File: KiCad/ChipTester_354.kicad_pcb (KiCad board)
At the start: 2 copper layers, 11 parts, among them U3 MCP6002-xP

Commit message: added footprints to schematic
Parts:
- removed U3: MCP6002-xP, Package_SO:SOIC-8_3.9x4.9mm_P1.27mm
- added C1: 0.33 µF, Capacitor_SMD:C_0201_0603Metric, F.Cu at (23.2, 61.0)
- added C2: 0.1 µF, Capacitor_SMD:C_0201_0603Metric, F.Cu at (23.2, 66.0)
- added D3: BLU, Diode_SMD:D_0201_0603Metric, F.Cu at (40.3, 66.0)
- added D4: WHT, Diode_SMD:D_0201_0603Metric, F.Cu at (39.6, 71.1)
- added D5: BLU, Diode_SMD:D_0201_0603Metric, F.Cu at (39.6, 76.2)
- added D6: WHT, Diode_SMD:D_0201_0603Metric, F.Cu at (39.6, 81.3)
- added R1: 510, Resistor_SMD:R_0201_0603Metric, F.Cu at (23.2, 81.3)
- added R2: 510, Resistor_SMD:R_0201_0603Metric, F.Cu at (23.2, 86.4)
- added U1: L7805, Package_TO_SOT_THT:TO-218-3_Vertical, F.Cu at (35.2, 59.1)
- added U2: AD623/INA126, Package_DIP:DIP-8_W7.62mm_Socket, F.Cu at (116.1, 39.2)
- added U6: TLE2426xP, Package_DIP:DIP-8_W7.62mm, F.Cu at (115.6, 25.4)
- added U7: TLE2426xP, Package_DIP:DIP-8_W7.62mm, F.Cu at (126.4, 25.4)
- added U8: TLE2426xP, Package_DIP:DIP-8_W7.62mm, F.Cu at (137.2, 25.4)
- R7: value 10k -> 20k
- R9: value 10k -> 7.5k
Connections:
- net /Wave Generator/WAVE renamed /WAVE

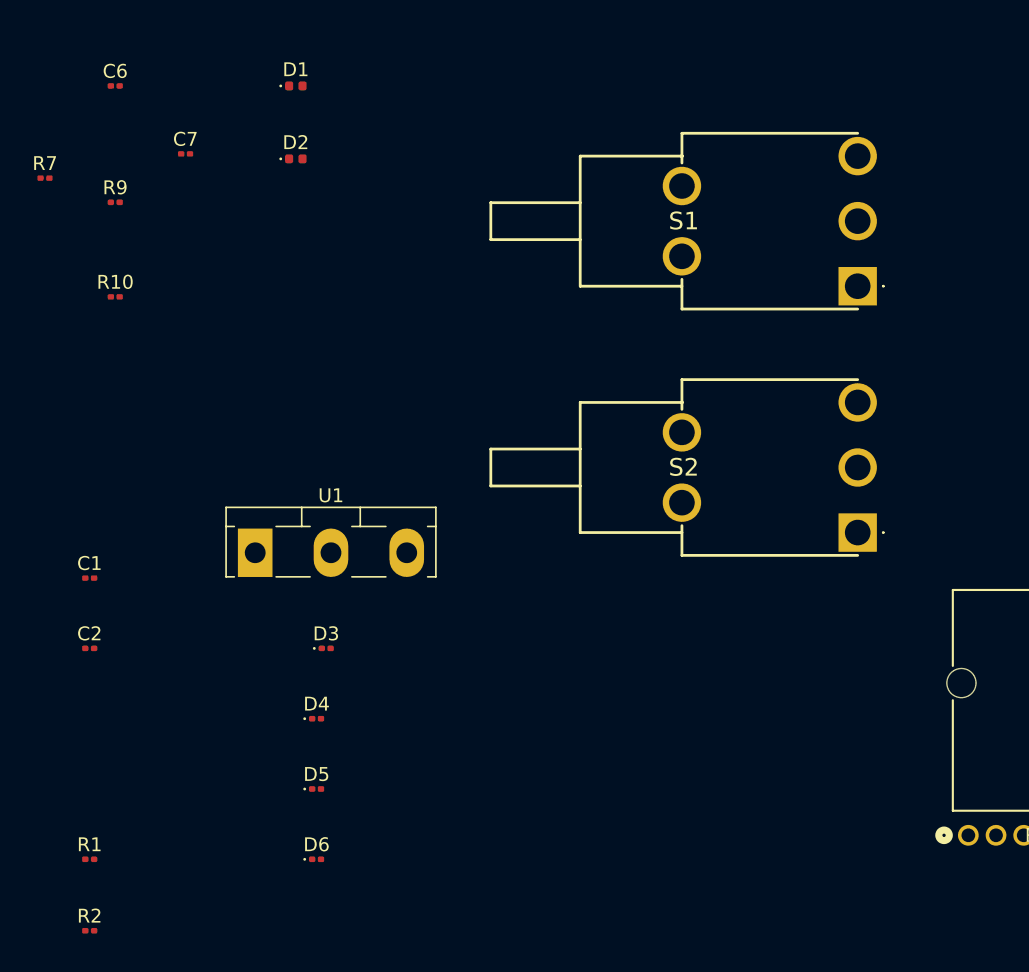
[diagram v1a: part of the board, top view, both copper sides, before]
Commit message: updated footprint to be all THT, battery holder still not there
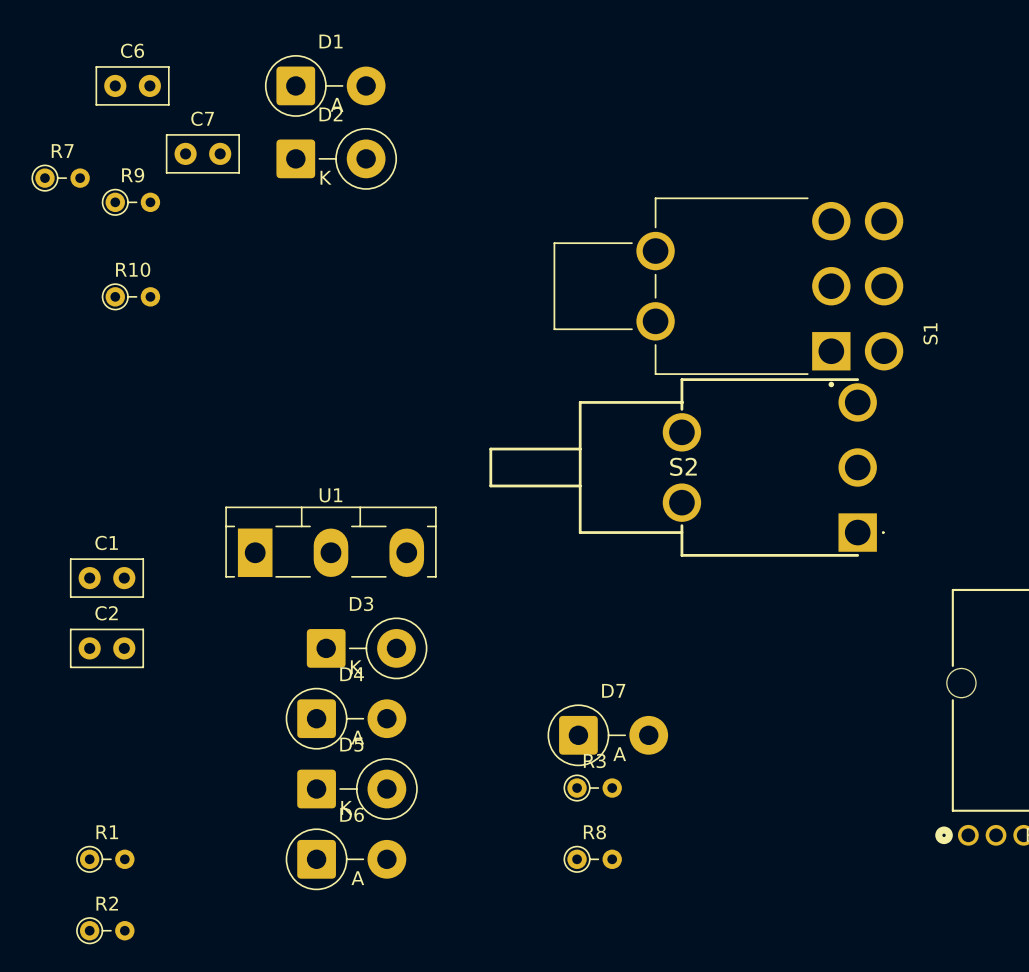
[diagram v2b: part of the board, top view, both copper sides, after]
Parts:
- added D7: GRN, Diode_THT:D_5W_P5.08mm_Vertical_AnodeUp, F.Cu at (58.5, 72.3)
- added R3: 1k, Resistor_THT:R_Axial_DIN0204_L3.6mm_D1.6mm_P2.54mm_Vertical, F.Cu at (58.4, 76.1)
- added R8: 20k, Resistor_THT:R_Axial_DIN0204_L3.6mm_D1.6mm_P2.54mm_Vertical, F.Cu at (58.4, 81.3)
- C1, C2, C6, C7: footprint Capacitor_SMD:C_0201_0603Metric -> Capacitor_THT:C_Disc_D5.0mm_W2.5mm_P2.50mm
- D1: footprint Diode_SMD:D_0402_1005Metric -> Diode_THT:D_5W_P5.08mm_Vertical_AnodeUp
- D2: footprint Diode_SMD:D_0402_1005Metric -> Diode_THT:D_5W_P5.08mm_Vertical_KathodeUp
- D3, D5: footprint Diode_SMD:D_0201_0603Metric -> Diode_THT:D_5W_P5.08mm_Vertical_KathodeUp
- D4, D6: footprint Diode_SMD:D_0201_0603Metric -> Diode_THT:D_5W_P5.08mm_Vertical_AnodeUp
- R1, R10, R2, R7, R9: footprint Resistor_SMD:R_0201_0603Metric -> Resistor_THT:R_Axial_DIN0204_L3.6mm_D1.6mm_P2.54mm_Vertical
- S1: value 100SP3T2B4M6RE -> 100DP1T2B4M6QE; footprint 100SP3T2B4M6RE:100SP3T2B4M6RE -> 100DP1T2B4M6QE:SW_100DP1T2B4M6QE
- turned S1 to 90 degrees
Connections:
- D4 pad 1: Net-(D3-A) -> /CHIP_GND
- D4 pad 2: /CHIP_GND -> Net-(D3-A)
- D6 pad 1: Net-(D5-A) -> /CHIP_GND
- D6 pad 2: /CHIP_GND -> Net-(D5-A)
- S1 pad 1: unconnected-(S1-N1-Pad1) -> +9V
- S1 pad 3: +9V -> unconnected-(S1-Pad3)

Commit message: Some TP -> Headers, added footprints, fixed battery footprint, started layout of board.
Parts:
- removed U6, U7, U8: TLE2426xP, Package_DIP:DIP-8_W7.62mm
- added BT_H1: BH9VPC, BH9VPC:BAT_BH9VPC, B.Cu at (240.5, 55.0)
- added C3: 0.1 µF, Capacitor_THT:C_Disc_D5.0mm_W2.5mm_P2.50mm, F.Cu at (-142.4, 102.9)
- added C4: 1 µF, Capacitor_THT:CP_Radial_D5.0mm_P2.00mm, F.Cu at (-3.41, -54.3)
- added C5: 1 µF, Capacitor_THT:CP_Radial_D5.0mm_P2.00mm, F.Cu at (-3.41, -47.7)
- added D10: BLU, Diode_THT:D_5W_P5.08mm_Vertical_KathodeUp, F.Cu at (-127.7, 5.95)
- added D11: WHT, Diode_THT:D_5W_P5.08mm_Vertical_AnodeUp, F.Cu at (-127.1, 11.4)
- added D12: BLU, Diode_THT:D_5W_P5.08mm_Vertical_KathodeUp, F.Cu at (-127.7, 16.9)
- added D13: WHT, Diode_THT:D_5W_P5.08mm_Vertical_AnodeUp, F.Cu at (-127.1, 22.4)
- added D8: BLU, Diode_THT:D_5W_P5.08mm_Vertical_KathodeUp, F.Cu at (-127.7, -4.99)
- added D9: WHT, Diode_THT:D_5W_P5.08mm_Vertical_AnodeUp, F.Cu at (-127.1, 0.48)
- added H1: MountingHole, MountingHole:MountingHole_3.2mm_M3, F.Cu at (-9.90, -35.4)
- added R11: 510, Resistor_THT:R_Axial_DIN0204_L3.6mm_D1.6mm_P2.54mm_Vertical, F.Cu at (-118.3, 12.0)
- added R4: 20k, Resistor_THT:R_Axial_DIN0204_L3.6mm_D1.6mm_P2.54mm_Vertical, F.Cu at (-104.0, 90.7)
- added R5: 50k, PRS12R_4025K_103B1:PRS12R-4_BRN, F.Cu at (202.7, -27.9)
- added TP1: VBATT-, TestPoint:TestPoint_Pad_D2.0mm, F.Cu at (-11.8, -55.5)
- added TP10: MCP_Out, Connector_PinSocket_2.54mm:PinSocket_1x03_P2.54mm_Vertical, F.Cu at (5.18, -55.2)
- added TP2: VBATT+, TestPoint:TestPoint_Pad_D2.0mm, F.Cu at (-11.8, -51.5)
- added TP3: 4.5V, TestPoint:TestPoint_Pad_D2.0mm, F.Cu at (-11.8, -47.4)
- added TP4: 5V+, TestPoint:TestPoint_Pad_D2.0mm, F.Cu at (-11.8, -43.4)
- added TP5: 0V (5V), TestPoint:TestPoint_Pad_D2.0mm, F.Cu at (-7.80, -55.5)
- added TP6: 4.5/2.25V VGND, TestPoint:TestPoint_Pad_D2.0mm, F.Cu at (-7.80, -51.5)
- added TP7: 2.5V VGND, TestPoint:TestPoint_Pad_D2.0mm, F.Cu at (-7.80, -47.4)
- added TP8: AD_Out, Connector_PinSocket_2.54mm:PinSocket_1x02_P2.54mm_Vertical, F.Cu at (-1.60, -37.0)
- added TP9: Wave, Connector_PinSocket_2.54mm:PinSocket_1x02_P2.54mm_Vertical, F.Cu at (5.00, -37.0)
- added U3: TLE2426xP, Package_DIP:DIP-8_W7.62mm, F.Cu at (-142.8, 91.2)
- added U4: TLE2426xP, Package_DIP:DIP-8_W7.62mm, F.Cu at (-132.0, 91.2)
- added U5: MCP6002-xP, Package_DIP:DIP-8_W7.62mm, F.Cu at (-95.9, 91.2)
- added U_T1: AD623/INA126, Package_DIP:DIP-8_W7.62mm_Socket, F.Cu at (165.7, 48.7)
- added U_T2: MCP6002-xP, Package_DIP:DIP-8_W7.62mm_Socket, F.Cu at (112.4, 60.2)
- C1: value 0.33 µF -> 1 µF; footprint Capacitor_THT:C_Disc_D5.0mm_W2.5mm_P2.50mm -> Capacitor_THT:CP_Radial_D5.0mm_P2.00mm
- C2: value 0.1 µF -> 0.33 µF
- D1: value 2.5V -> GRN
- D2: value 2.5V -> BLU
- D3, D5: value BLU -> WHT; footprint Diode_THT:D_5W_P5.08mm_Vertical_KathodeUp -> Diode_THT:D_5W_P5.08mm_Vertical_AnodeUp
- D4: value WHT -> BLU; footprint Diode_THT:D_5W_P5.08mm_Vertical_AnodeUp -> Diode_THT:D_5W_P5.08mm_Vertical_KathodeUp
- D6: value WHT -> 2.5V; footprint Diode_THT:D_5W_P5.08mm_Vertical_AnodeUp -> Diode_THT:D_5W_P5.08mm_Vertical_KathodeUp
- D7: value GRN -> 2.5V
- R1: value 510 -> 1k
- R10: value 3.3k -> 510
- R3: value 1k -> 510
- R6: value 50k -> 20k; footprint PRS12R_4025K_103B1:PRS12R-4_BRN -> Resistor_THT:R_Axial_DIN0204_L3.6mm_D1.6mm_P2.54mm_Vertical
- R7: value 20k -> 7.5k
- R8: value 20k -> 3.3k
- R9: value 7.5k -> 510
- U1: value L7805 -> TLE2426xP; footprint Package_TO_SOT_THT:TO-218-3_Vertical -> Package_DIP:DIP-8_W7.62mm
- U2: value AD623/INA126 -> L7805; footprint Package_DIP:DIP-8_W7.62mm_Socket -> Package_TO_SOT_THT:TO-218-3_Vertical
- moved D1 181.1 mm to (219.2, 26.0)
- moved U1 171.8 mm to (204.3, 29.2), turned to -90 degrees
- moved S1 160.6 mm to (239.1, 31.2), turned to -90 degrees
- moved S2 151.8 mm to (172.7, -61.5), turned to 90 degrees
- moved R10 146.8 mm to (-118.3, 8.83)
- moved R9 146.1 mm to (-118.3, 5.68)
- moved U2 79.3 mm to (119.5, -40.0), turned to 90 degrees
- moved D2 35.8 mm to (38.1, 66.5)
- moved D6 10.9 mm to (34.7, 91.0)
- moved D3 7.74 mm to (38.2, 73.5)
- moved D4 7.74 mm to (37.5, 78.6)
- moved D5 7.74 mm to (37.5, 83.7)
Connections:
- C1 pad 1: +9V -> GND
- C1 pad 2: GND -> Net-(U1-NOISE_REDUCTION)
- C2 pad 1: +5V -> +9V
- C7 pad 1: Net-(U4A-+) -> Net-(U5A-+)
- C7 pad 2: /PWR Supply/2.5V VGND -> /2.5 VGND
- D1 pad 1: Net-(D1-K) -> GND
- D2 pad 1: /WAVE -> /CHIP_GND
- D2 pad 2: Net-(D1-A) -> Net-(D2-A)
- D3 pad 2: Net-(D3-A) -> Net-(D2-A)
- D4 pad 2: Net-(D3-A) -> Net-(D4-A)
- D5 pad 2: Net-(D5-A) -> Net-(D4-A)
- D6 pad 1: /CHIP_GND -> /WAVE
- D6 pad 2: Net-(D5-A) -> Net-(D6-A)
- D7 pad 1: GND -> Net-(D7-K)
- D7 pad 2: Net-(D7-A) -> Net-(D6-A)
- R1 pad 1: /WAVE -> +9V
- R1 pad 2: Net-(D3-A) -> Net-(D1-A)
- R10 pad 1: Net-(D1-K) -> Net-(D10-A)
- R10 pad 2: /PWR Supply/2.5V VGND -> /MCP6002 and IF353/MCPA_O
- R2 pad 1: Net-(D5-A) -> /WAVE
- R2 pad 2: Net-(R2-Pad2) -> Net-(D2-A)
- R3 pad 1: +9V -> Net-(D4-A)
- R3 pad 2: Net-(D7-A) -> /AD623 and INA126/AD_O
- R6 pad 1: Net-(R6-Pad1) -> Net-(R5-Pad5)
- R6 pad 2: Net-(U4A-+) -> /2.5 VGND
- R7 pad 1: Net-(C6-Pad2) -> /WAVE
- R7 pad 2: Net-(R6-Pad1) -> Net-(D7-K)
- R8 pad 1: Net-(R6-Pad5) -> Net-(D7-K)
- R8 pad 2: /PWR Supply/2.5V VGND -> /2.5 VGND
- R9 pad 1: /WAVE -> Net-(D8-A)
- R9 pad 2: Net-(D1-K) -> /WAVE
- S1 pad 1: +9V -> unconnected-(S1-Pad1)
- S1 pad 3: unconnected-(S1-Pad3) -> +9V
- S1 pad 4: GND -> unconnected-(S1-Pad4)
- S1 pad 6: unconnected-(S1-Pad6) -> GND
- S1 pad S1: (no net) -> unconnected-(S1-PadS1)
- S1 pad S2: (no net) -> unconnected-(S1-PadS2)
- U1 pad 1: +9V -> /PWR Supply/VDIV
- U1 pad 3: +5V -> +9V
- U2 pad 1: unconnected-(U2-Rg-Pad1) -> +9V
- U2 pad 2: unconnected-(U2---Pad2) -> GND
- U2 pad 3: /WAVE -> +5V

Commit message: Made the board :D
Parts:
- added H2: MountingHole, MountingHole:MountingHole_3.2mm_M3, F.Cu at (68.9, 111.5)
- added H3: MountingHole, MountingHole:MountingHole_3.2mm_M3, F.Cu at (68.9, 57.0)
- added H4: MountingHole, MountingHole:MountingHole_3.2mm_M3, F.Cu at (233.9, 111.5)
- D1, D11, D13, D3, D5, D9: footprint Diode_THT:D_5W_P5.08mm_Vertical_AnodeUp -> LED_THT:LED_D5.0mm
- D10, D12, D2, D4, D8: footprint Diode_THT:D_5W_P5.08mm_Vertical_KathodeUp -> LED_THT:LED_D5.0mm
- D6: footprint Diode_THT:D_5W_P5.08mm_Vertical_KathodeUp -> Diode_THT:D_DO-35_SOD27_P7.62mm_Horizontal
- D7: footprint Diode_THT:D_5W_P5.08mm_Vertical_AnodeUp -> Diode_THT:D_DO-35_SOD27_P7.62mm_Horizontal
- R1, R10, R11, R2, R3, R4, R6, R7, R8, R9: footprint Resistor_THT:R_Axial_DIN0204_L3.6mm_D1.6mm_P2.54mm_Vertical -> Resistor_THT:R_Axial_DIN0207_L6.3mm_D2.5mm_P7.62mm_Horizontal
- TP1: moved to B.Cu
- U2: footprint Package_TO_SOT_THT:TO-218-3_Vertical -> Package_TO_SOT_THT:TO-218-3_Horizontal_TabDown
- moved C3 355.0 mm to (209.9, 58.2), turned to -90 degrees
- moved U4 296.7 mm to (163.7, 66.3), turned to 180 degrees
- moved R4 272.0 mm to (167.9, 85.5), turned to 180 degrees
- moved U5 267.4 mm to (171.2, 79.6)
- moved U3 260.9 mm to (117.4, 71.8), turned to 180 degrees
- moved H1 260.7 mm to (233.9, 57.0)
- moved TP1 248.2 mm to (200.4, 73.2)
- moved D9 240.1 mm to (87.8, 107.5)
- moved D13 240.1 mm to (97.3, 107.5)
- moved D12 240.0 mm to (97.3, 100.5)
- moved R11 240.0 mm to (103.4, 104.0), turned to 90 degrees
- moved D8 239.9 mm to (87.8, 100.5)
- moved R9 233.8 mm to (93.9, 104.0), turned to 90 degrees
- moved D11 226.8 mm to (78.3, 107.5)
- moved D10 226.7 mm to (78.3, 100.5)
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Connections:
- TP10 pad 1: /BATT- -> GND
- U_T2 pad 4: /BATT- -> GND
- U_T2 pad 8: /BATT+ -> +9V
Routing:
- net +9V: track 0.00 -> 159.6 mm
- net /2.5 VGND: track 0.00 -> 131.3 mm
- net /WAVE: track 0.00 -> 115.9 mm
- net +5V: track 0.00 -> 76.0 mm
- net /CHIP_GND: track 0.00 -> 59.5 mm
- net /PWR Supply/VDIV: track 0.00 -> 47.9 mm
- net Net-(D7-K): track 0.00 -> 39.8 mm
- net /BATT-: track 0.00 -> 38.9 mm
- net Net-(U5A-+): track 0.00 -> 31.0 mm
- net /MCP6002 and IF353/MCPA_O: track 0.00 -> 29.8 mm
- net /MCP6002 and IF353/MCPB_O: track 0.00 -> 29.6 mm
- net /CHIP+: track 0.00 -> 26.5 mm
- net Net-(D2-A): track 0.00 -> 24.3 mm
- net /BATT+: track 0.00 -> 22.1 mm
- net /AD623 and INA126/AD_O: track 0.00 -> 21.3 mm
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- added copper zone on B.Cu, net GND
- added copper zone on F.Cu, net GND
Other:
- board outline added: 172 x 61.5 mm
- board text added: "AD623 INA126"
- board text added: "MCP6002 & LF353"

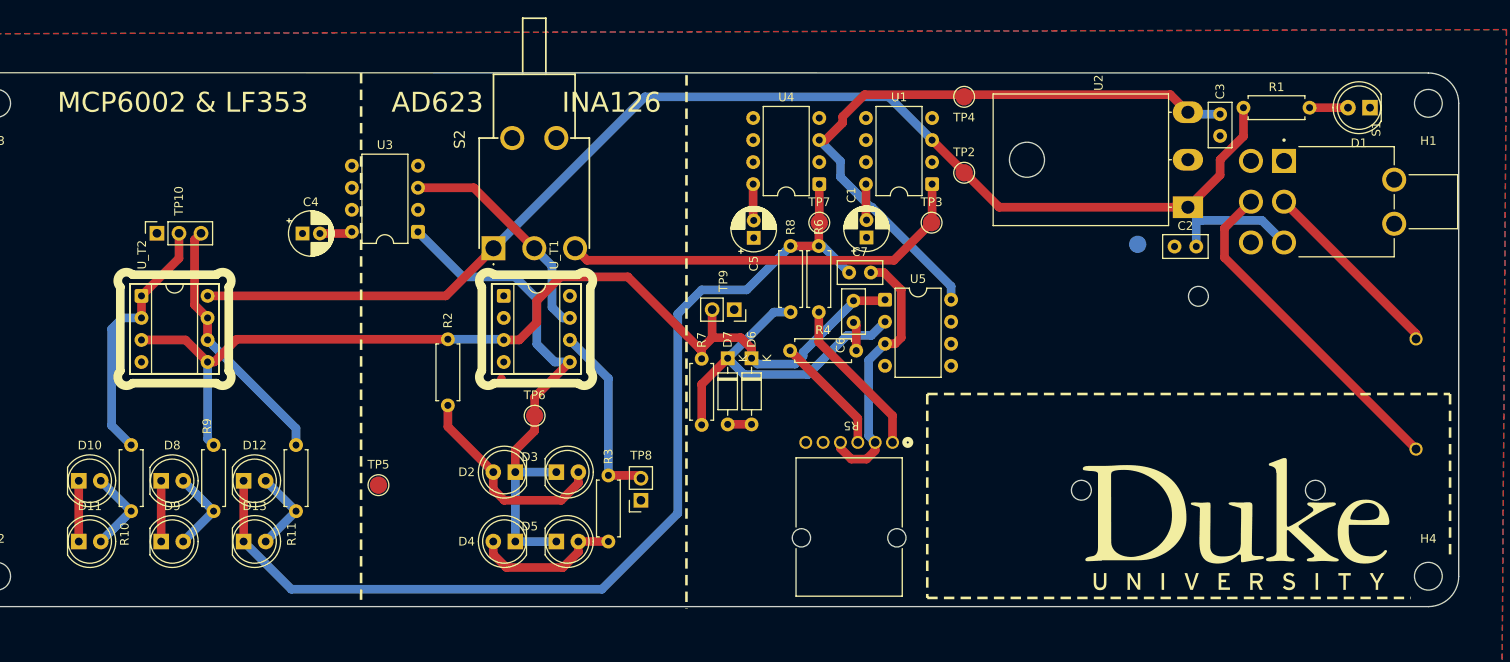
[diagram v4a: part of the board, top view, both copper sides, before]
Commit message: Added annotations to pcb
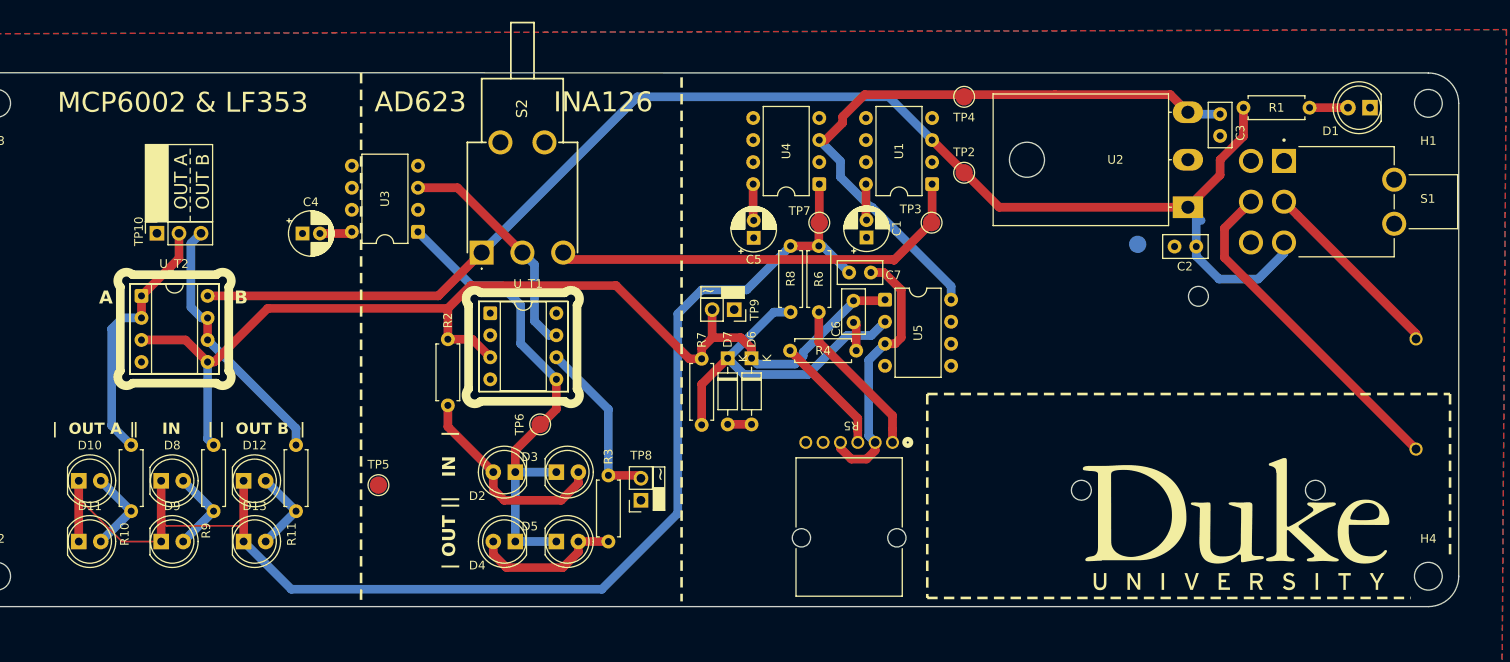
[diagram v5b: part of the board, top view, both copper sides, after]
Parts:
- moved U_T1 2.53 mm to (125.8, 81.2)
- moved S2 1.45 mm to (124.8, 74.2)
- moved TP6 1.18 mm to (131.5, 94.0), turned to 90 degrees
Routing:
- net /2.5 VGND: track 131.3 -> 152.7 mm
- net +5V: track 76.0 -> 86.5 mm
- net /WAVE: track 115.9 -> 123.6 mm
- net +9V: track 159.6 -> 164.6 mm
- net /CHIP_GND: track 59.5 -> 56.5 mm
- net /BATT+: track 22.1 -> 24.4 mm
- net Net-(R5-Pad5): track 18.5 -> 20.1 mm
- net /BATT-: track 38.9 -> 40.4 mm
- net Net-(R4-Pad2): track 13.8 -> 15.2 mm
- net /AD623 and INA126/AD_O: track 21.3 -> 20.0 mm
- net /PWR Supply/VDIV: track 47.9 -> 49.1 mm
- net Net-(U5A-+): track 31.0 -> 31.8 mm
- net /MCP6002 and IF353/MCPB_O: track 29.6 -> 30.3 mm
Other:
- board text added: "A"
- board text added: "B"
- board text added: "OUT A"
- board text added: "OUT B"
- board text added: "| IN |"
- board text added: "| OUT A |"
- board text added: "| OUT B |"
- board text added: "| OUT |"
- board text added: "~"
